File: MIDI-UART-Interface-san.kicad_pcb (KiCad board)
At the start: 2 copper layers, 56 x 32 mm, 36 parts, among them CN1 Conn_01x04_Female, J1 AudioJack3, J2 AudioJack3, J3 Conn_01x03_Female, J4 Conn_01x03_Female, U1 CD74HC4050PWR, U2 TLP2361_TPL_E

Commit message: replace pcb w/ renamed footprints.
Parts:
- J1, J2: footprint MIDI-Interface-san:3.5mm_Stereo_TRS_PJ-3210-4A_and_ST-005-G -> MIDI-UART-Interface-san:3.5mm_Stereo_TRS_PJ-3210-4A_and_ST-005-G
- R10: value 10k -> 1k
- TP1, TP2, TP3, TP4, TP5: footprint my_footprint:TP_1PAD -> MIDI-UART-Interface-san:TP_1PAD
- U1: footprint MIDI-Interface-san:SOP65P640X120-16N -> MIDI-UART-Interface-san:SOP65P640X120-16N

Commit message: update to kicad 6.0.2
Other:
- net class Default removed

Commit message: Update to revision 2
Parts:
- removed ? (x2): , my_footprint:yajirushi-800dpi_3_6x1_3mm
- added U3: BAS40DW-04-7-F, MIDI-UART-Interface-san:SOT-363_DIO, F.Cu at (145.7, 98.0)
- U1: value CD74HC4050PWR -> CD74HC4050PWR/74HC4050PW
- moved J1 0.05 mm to (136.0, 92.1)
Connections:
- D1 pad 2: Net-(D1-Pad2) -> A1
- J1 pad R: Net-(J1-PadR) -> in_R
- J1 pad S: (no net) -> unconnected-(J1-PadS)
- J1 pad T: Net-(D1-Pad2) -> in_T
- R4 pad 2: Net-(J1-PadR) -> C1
- U1 pad 13: (no net) -> unconnected-(U1-NC_13-Pad13)
- U1 pad 15: (no net) -> unconnected-(U1-6Y-Pad15)
- U1 pad 16: (no net) -> unconnected-(U1-NC_16-Pad16)
- U1 pad 6: (no net) -> unconnected-(U1-3Y-Pad6)
- U2 pad 3: Net-(D1-Pad2) -> A1
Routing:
- net Net-(D1-Pad2): track 27.2 -> 0.00 mm
- net C1: track 0.00 -> 21.0 mm, vias 0 -> 2
- net A1: track 0.00 -> 17.7 mm, vias 0 -> 2
- net in_R: track 0.00 -> 14.1 mm, vias 0 -> 2
- net in_T: track 0.00 -> 12.2 mm
- net Net-(J1-PadR): track 5.99 -> 0.00 mm
- net midi_in_led: track 30.3 -> 29.2 mm
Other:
- board text added: "MIDI-UART Interface-san rev.2 2024 Kinoshita Lab."
- board text removed: "Holes: 4-Φ3.2mm"
- board text removed: "MIDI-UART Interface-san 2021 Kinoshita Lab."

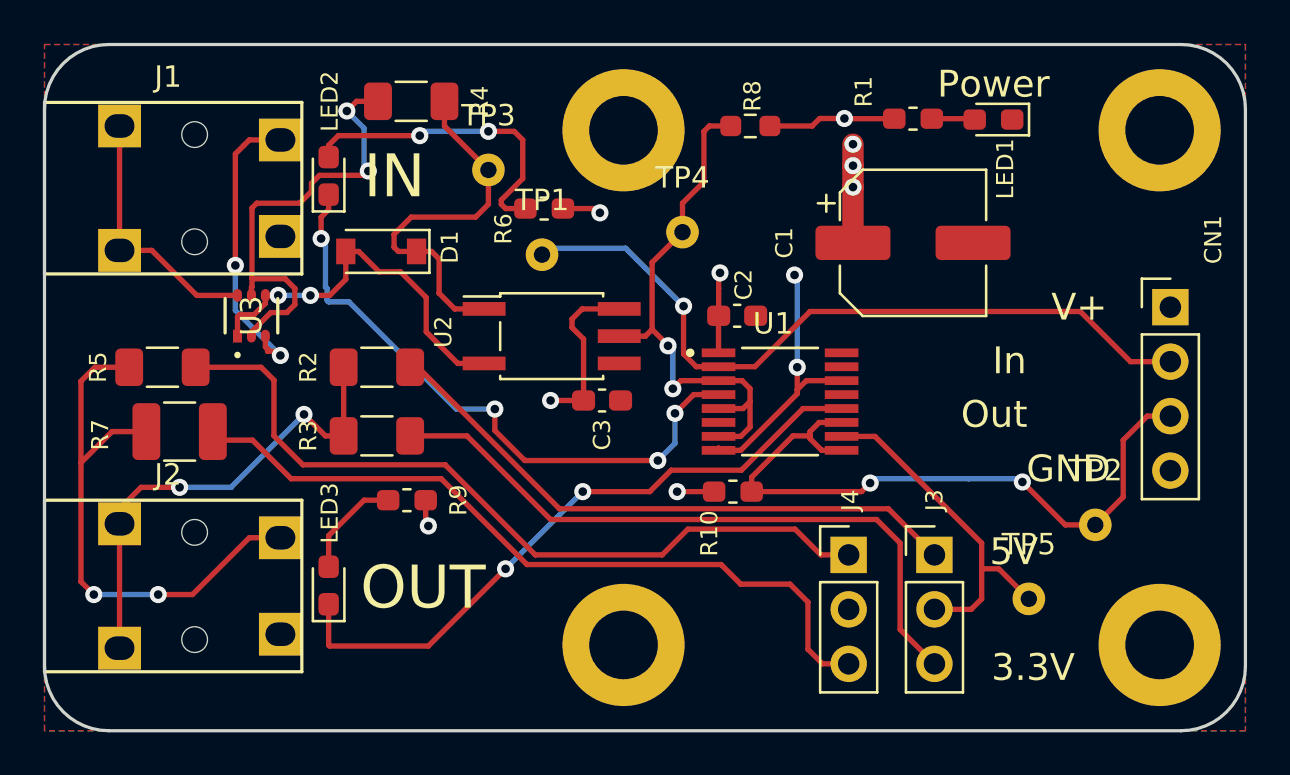
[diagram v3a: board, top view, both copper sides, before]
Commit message: Revise to 2.1, KiCad 9.0
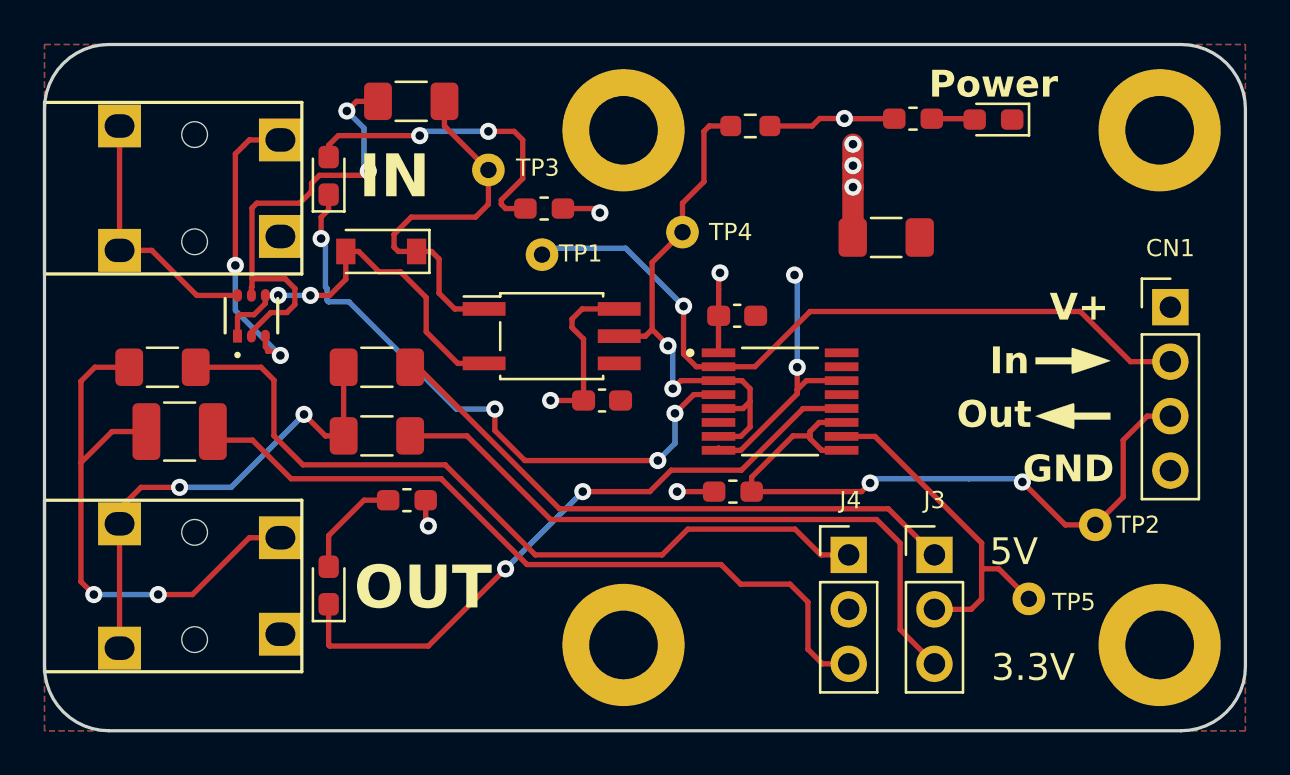
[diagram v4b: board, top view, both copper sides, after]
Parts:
- added ?: , my_footprint:yajirushi-800dpi_3_6x1_3mm, F.Cu at (184.0, 100.2)
- added ?: , my_footprint:yajirushi-800dpi_3_6x1_3mm, F.Cu at (183.9, 102.7)
- C1: value 100u -> 100u 6.3V; footprint Capacitor_SMD:CP_Elec_6.3x5.3 -> Capacitor_SMD:C_1206_3216Metric_Pad1.33x1.80mm_HandSolder
- J1: footprint MIDI-UART-Interface-san:3.5mm_Stereo_TRS_PJ-3210-4A_and_ST-005-G -> my_footprint:3.5mm_Stereo_TRS_PJ-3210-4A_and_ST-005-G
- J2: footprint MIDI-UART-Interface-san:3.5mm_Stereo_TRS_PJ-3210-4A_and_ST-005-G -> MIDI-Interface-san:3.5mm_Stereo_TRS_PJ-3210-4A_and_ST-005-G
- TP1, TP2, TP3, TP4, TP5: footprint MIDI-UART-Interface-san:TP_1PAD -> my_footprint:TP_1PAD
- U1: footprint MIDI-UART-Interface-san:SOP65P640X120-16N -> MIDI-Interface-san:SOP65P640X120-16N
- U3: footprint MIDI-UART-Interface-san:SOT-363_DIO -> ultra_librarian:SOT-363_DIO
- moved C1 1.27 mm to (175.2, 94.4)
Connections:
- net C1 renamed BRIDGED IN R
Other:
- board text added: "MIDI-UART Interface-san rev.2.1 2024 Kinoshita Lab."
- board text removed: "MIDI-UART Interface-san rev.2 2024 Kinoshita Lab."
